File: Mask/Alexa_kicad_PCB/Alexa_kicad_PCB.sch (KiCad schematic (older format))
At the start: 38 parts, among them J1 Jack-DC, J2 USB_B_Micro, J3 Conn_01x07_Male, M1 Motor_Servo, M2 Motor_Servo, M3 Motor_Servo, U1 TLV2372, U2 LM1117-3.3, U3 STM32F405RGTx, X1 1503_09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

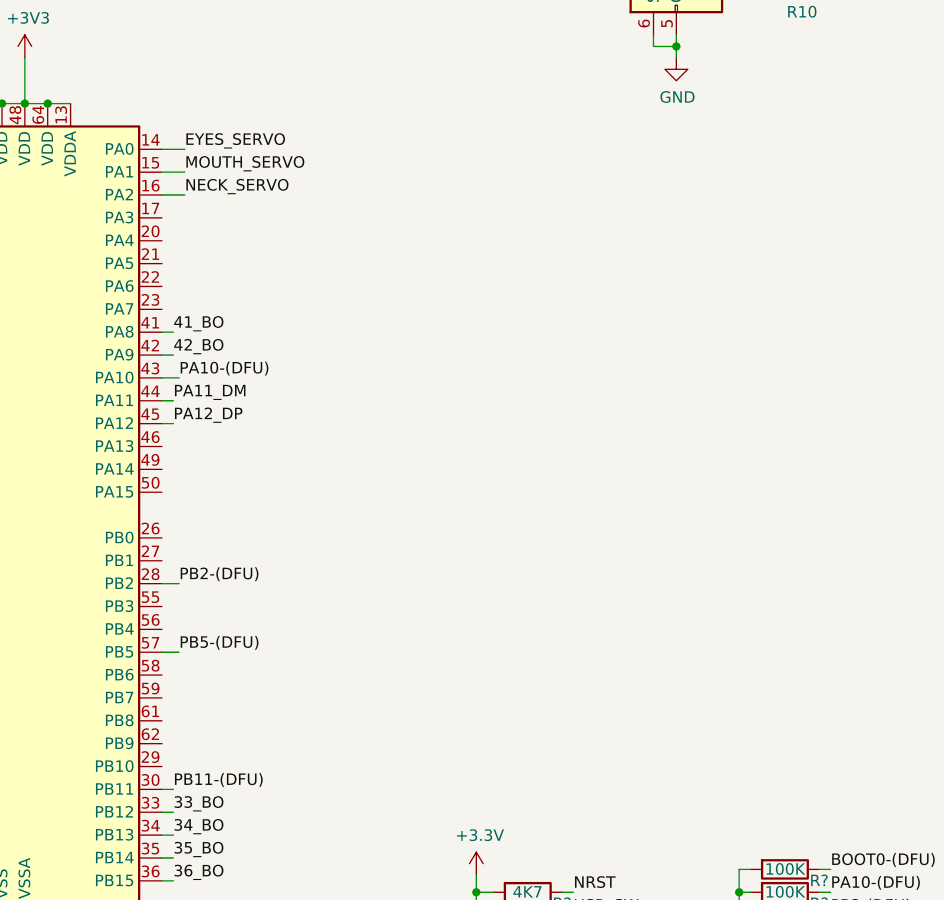
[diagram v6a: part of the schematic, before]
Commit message: added pwr + indication leds
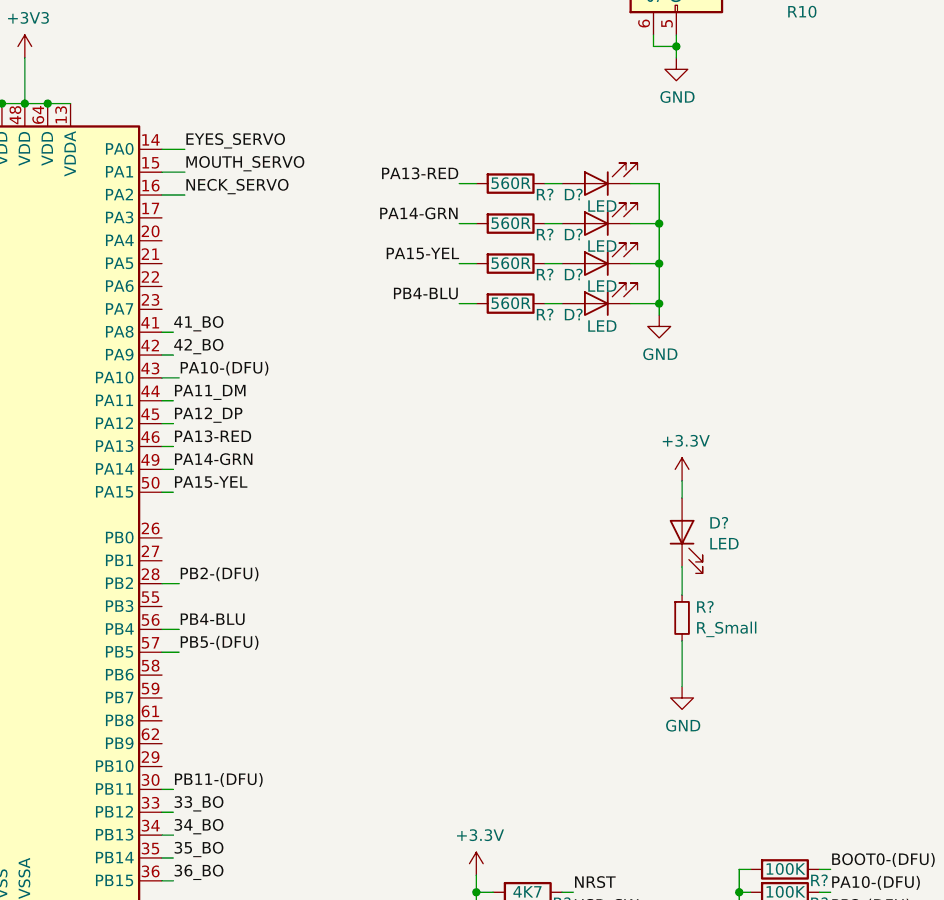
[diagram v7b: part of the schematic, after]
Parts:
- added D? (x5): LED, symbol Device:LED
- added R?: R_Small, symbol Device:R_Small
- added R? (x4): 560R, symbol Device:R
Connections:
- net +3V3: now also D?.2 (A)
- net GND: now also D?.1 (K), D?.1 (K), D?.1 (K), D?.1 (K), R?.2
- net PA13-RED: now reaches U3.46 (PA13)
- net PA13-RED: now also R?.2
- net PA14-GRN: now reaches U3.49 (PA14)
- net PA14-GRN: now also R?.2
- net PA15-YEL: now reaches U3.50 (PA15)
- net PA15-YEL: now also R?.2
- net PB4-BLU: now reaches U3.56 (PB4)
- net PB4-BLU: now also R?.2
- new net: D?.1 (K), R?.1
- new net: D?.2 (A), R?.1 (x4)
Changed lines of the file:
@@
 Wire Wire Line
 	3400 2825 3400 2875
+$Comp
+L power:+3.3V #PWR?
+U 1 1 5F7FA193
+P 7625 3700
+F 0 "#PWR?" H 7625 3550 50  0001 C CNN
+F 1 "+3.3V" H 7640 3873 50  0000 C CNN
+F 2 "" H 7625 3700 50  0001 C CNN
+F 3 "" H 7625 3700 50  0001 C CNN
+	1    7625 3700
+	1    0    0    -1
+$EndComp
+$Comp
+L Device:LED D?
+U 1 1 5F7FC16D
+P 7625 3925
+F 0 "D?" V 7664 3808 50  0000 R CNN
+F 1 "LED" V 7573 3808 50  0000 R CNN
+F 2 "" H 7625 3925 50  0001 C CNN
+F 3 "~" H 7625 3925 50  0001 C CNN
+	1    7625 3925
+	0    -1   -1   0
+$EndComp
+$Comp
+L Device:R_Small R?
+U 1 1 5F7FDB46
+P 7625 4300
+F 0 "R?" H 7684 4346 50  0000 L CNN
+F 1 "R_Small" H 7684 4255 50  0000 L CNN
+F 2 "" H 7625 4300 50  0001 C CNN
+F 3 "~" H 7625 4300 50  0001 C CNN
+	1    7625 4300
+	1    0    0    -1
+$EndComp
+$Comp
+L power:GND #PWR?
+U 1 1 5F8001A1
+P 7625 4600
+F 0 "#PWR?" H 7625 4350 50  0001 C CNN
+F 1 "GND" H 7630 4427 50  0000 C CNN
+F 2 "" H 7625 4600 50  0001 C CNN
+F 3 "" H 7625 4600 50  0001 C CNN
+	1    7625 4600
+	1    0    0    -1
+$EndComp
+Wire Wire Line
+	7625 3700 7625 3775
+Wire Wire Line
+	7625 4075 7625 4200
+Wire Wire Line
+	7625 4400 7625 4600
+Text Label 5400 3650 0    50   ~ 0
+PA14-GRN
+Text Label 5400 3750 0    50   ~ 0
+PA15-YEL
+Wire Wire Line
+	5350 3550 5400 3550
+Wire Wire Line
+	5350 3650 5400 3650
+Wire Wire Line
+	5350 3750 5400 3750
+Text Label 5425 4350 0    50   ~ 0
+PB4-BLU
+Wire Wire Line
+	5350 4350 5425 4350
+$Comp
+L Device:LED D?
+U 1 1 5F8409F6
+P 7250 2400
+F 0 "D?" H 7350 2450 50  0000 C CNN
+F 1 "LED" H 7225 2500 50  0000 C CNN
+F 2 "" H 7250 2400 50  0001 C CNN
+F 3 "~" H 7250 2400 50  0001 C CNN
+	1    7250 2400
+	-1   0    0    1
+$EndComp
+$Comp
+L power:GND #PWR?
+U 1 1 5F8413CA
+P 7525 2975
+F 0 "#PWR?" H 7525 2725 50  0001 C CNN
+F 1 "GND" H 7530 2802 50  0000 C CNN
+F 2 "" H 7525 2975 50  0001 C CNN
+F 3 "" H 7525 2975 50  0001 C CNN
+	1    7525 2975
+	1    0    0    -1
+$EndComp
+$Comp
+L Device:LED D?
+U 1 1 5F845BD5
+P 7250 2575
+F 0 "D?" H 7350 2625 50  0000 C CNN
+F 1 "LED" H 7225 2675 50  0000 C CNN
+F 2 "" H 7250 2575 50  0001 C CNN
+F 3 "~" H 7250 2575 50  0001 C CNN
+	1    7250 2575
+	-1   0    0    1
+$EndComp
+$Comp
+L Device:LED D?
+U 1 1 5F8463D3
+P 7250 2750
+F 0 "D?" H 7350 2800 50  0000 C CNN
+F 1 "LED" H 7225 2850 50  0000 C CNN
+F 2 "" H 7250 2750 50  0001 C CNN
+F 3 "~" H 7250 2750 50  0001 C CNN
+	1    7250 2750
+	-1   0    0    1
+$EndComp
+$Comp
+L Device:LED D?
+U 1 1 5F846EAD
+P 7250 2925
+F 0 "D?" H 7350 2975 50  0000 C CNN
+F 1 "LED" H 7225 3025 50  0000 C CNN
+F 2 "" H 7250 2925 50  0001 C CNN
+F 3 "~" H 7250 2925 50  0001 C CNN
+	1    7250 2925
+	-1   0    0    1
+$EndComp
+$Comp
+L Device:R R?
+U 1 1 5F84B5C8
+P 6875 2400
+F 0 "R?" V 6925 2550 50  0000 C CNN
+F 1 "560R" V 6875 2400 50  0000 C CNN
+F 2 "" V 6805 2400 50  0001 C CNN
+F 3 "~" H 6875 2400 50  0001 C CNN
+	1    6875 2400
+	0    1    1    0
+$EndComp
+$Comp
+L Device:R R?
+U 1 1 5F84D4CF
+P 6875 2575
+F 0 "R?" V 6925 2725 50  0000 C CNN
+F 1 "560R" V 6875 2575 50  0000 C CNN
+F 2 "" V 6805 2575 50  0001 C CNN
+F 3 "~" H 6875 2575 50  0001 C CNN
+	1    6875 2575
+	0    1    1    0
+$EndComp
+$Comp
+L Device:R R?
+U 1 1 5F84D853
+P 6875 2750
+F 0 "R?" V 6925 2900 50  0000 C CNN
+F 1 "560R" V 6875 2750 50  0000 C CNN
+F 2 "" V 6805 2750 50  0001 C CNN
+F 3 "~" H 6875 2750 50  0001 C CNN
+	1    6875 2750
+	0    1    1    0
+$EndComp
+$Comp
+L Device:R R?
+U 1 1 5F84DB29
+P 6875 2925
+F 0 "R?" V 6925 3075 50  0000 C CNN
+F 1 "560R" V 6875 2925 50  0000 C CNN
+F 2 "" V 6805 2925 50  0001 C CNN
+F 3 "~" H 6875 2925 50  0001 C CNN
+	1    6875 2925
+	0    1    1    0
+$EndComp
+Text Label 5400 3550 0    50   ~ 0
+PA13-RED
+Text Label 6650 2400 2    50   ~ 0
+PA13-RED
+Text Label 6650 2575 2    50   ~ 0
+PA14-GRN
+Text Label 6650 2750 2    50   ~ 0
+PA15-YEL
+Text Label 6650 2925 2    50   ~ 0
+PB4-BLU
+Wire Wire Line
+	6650 2400 6725 2400
+Wire Wire Line
+	6650 2575 6725 2575
+Wire Wire Line
+	6650 2750 6725 2750
+Wire Wire Line
+	6650 2925 6725 2925
+Wire Wire Line
+	7025 2400 7100 2400
+Wire Wire Line
+	7025 2575 7100 2575
+Wire Wire Line
+	7025 2750 7100 2750
+Wire Wire Line
+	7025 2925 7100 2925
+Wire Wire Line
+	7400 2400 7525 2400
+Wire Wire Line
+	7525 2400 7525 2575
+Wire Wire Line
+	7400 2575 7525 2575
+Connection ~ 7525 2575
+Wire Wire Line
+	7525 2575 7525 2750
+Wire Wire Line
+	7400 2750 7525 2750
+Connection ~ 7525 2750
+Wire Wire Line
+	7525 2750 7525 2925
+Wire Wire Line
+	7400 2925 7525 2925
+Connection ~ 7525 2925
+Wire Wire Line
+	7525 2925 7525 2975
 $EndSCHEMATC

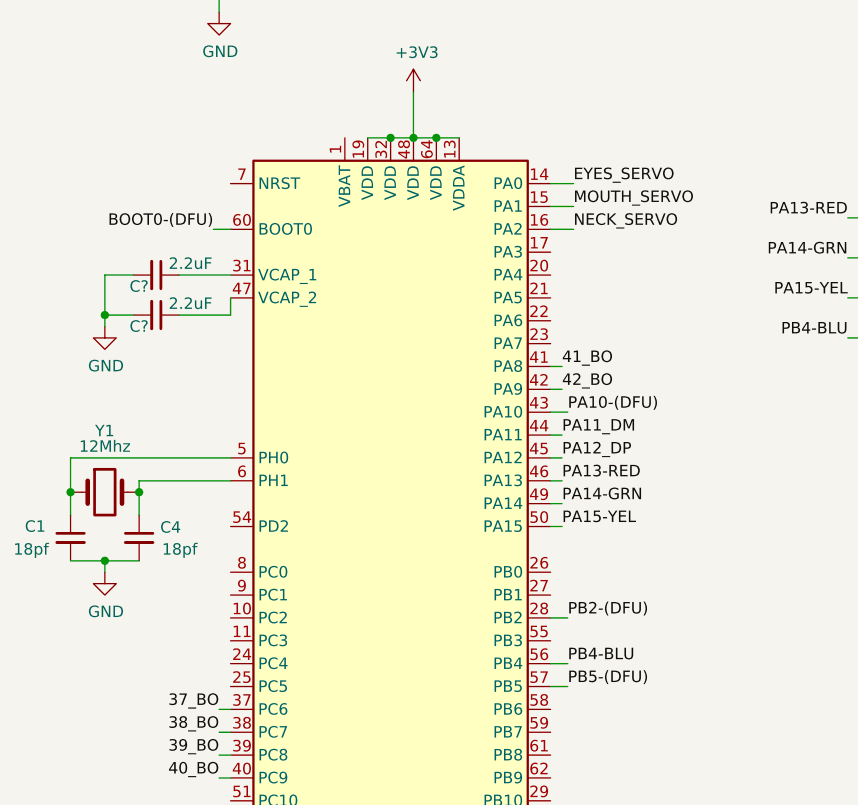
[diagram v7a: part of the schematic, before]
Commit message: ADDED LABS NRST AND USR_SW
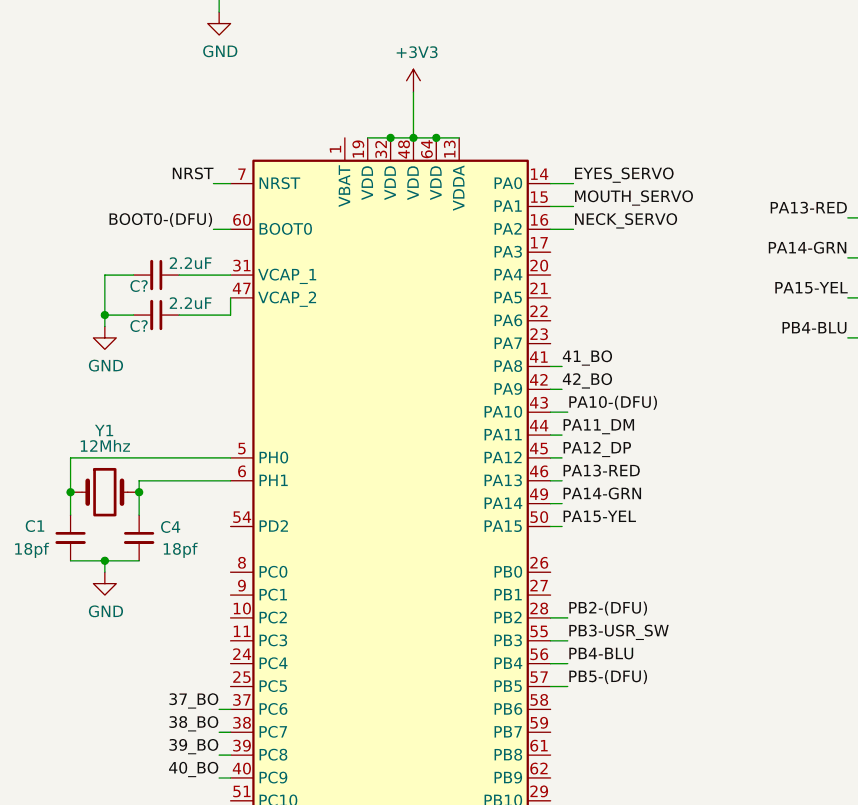
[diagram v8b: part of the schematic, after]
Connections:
- net NRST: now also U3.7 (NRST)
- net PB3-USR_SW: now reaches U3.55 (PB3)
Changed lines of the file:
@@
 Wire Wire Line
 	7525 2925 7525 2975
+Text Label 3875 2250 2    50   ~ 0
+NRST
+Wire Wire Line
+	3875 2250 3950 2250
+Text Label 5425 4250 0    50   ~ 0
+PB3-USR_SW
+Wire Wire Line
+	5350 4250 5425 4250
 $EndSCHEMATC
